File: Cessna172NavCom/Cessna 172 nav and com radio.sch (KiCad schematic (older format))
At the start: 33 parts, among them J2 USB_B_Micro, J8 Conn_02x20_Odd_Even, SW1 SW_Push, SW2 SW_Push, SW3 SW_Push, SW4 SW_Push, SW5 SW_Push, SW6 SW_Push

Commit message: Fully routed!!!
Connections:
- net GND: now also J8.27 (Pin_27), J8.28 (Pin_28), J8.29 (Pin_29), J8.30 (Pin_30)
- no-connect marks 11 -> 7
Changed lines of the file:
@@
 	1    0    0    -1
 $EndComp
-NoConn ~ 8650 1500
-NoConn ~ 8750 1500
-NoConn ~ 8750 2000
-NoConn ~ 8650 2000
 $Comp
-L power:+5V #PWR?
+L power:+5V #PWR0101
 U 1 1 5F695056
 P 2050 3500
-F 0 "#PWR?" H 2050 3350 50  0001 C CNN
+F 0 "#PWR0101" H 2050 3350 50  0001 C CNN
 F 1 "+5V" V 2065 3628 50  0000 L CNN
 F 2 "" H 2050 3500 50  0001 C CNN
@@
 $EndComp
 $Comp
-L power:GND #PWR?
+L power:GND #PWR0102
 U 1 1 5F6951C0
 P 2050 3800
-F 0 "#PWR?" H 2050 3550 50  0001 C CNN
+F 0 "#PWR0102" H 2050 3550 50  0001 C CNN
 F 1 "GND" V 2055 3672 50  0000 R CNN
 F 2 "" H 2050 3800 50  0001 C CNN
@@
 	0    1    1    0
 $EndComp
+$Comp
+L power:GND #PWR?
+U 1 1 5F67D432
+P 8650 1500
+F 0 "#PWR?" H 8650 1250 50  0001 C CNN
+F 1 "GND" H 8655 1327 50  0000 C CNN
+F 2 "" H 8650 1500 50  0001 C CNN
+F 3 "" H 8650 1500 50  0001 C CNN
+	1    8650 1500
+	-1   0    0    1
+$EndComp
+$Comp
+L power:GND #PWR?
+U 1 1 5F67D9D0
+P 8750 1450
+F 0 "#PWR?" H 8750 1200 50  0001 C CNN
+F 1 "GND" H 8755 1277 50  0000 C CNN
+F 2 "" H 8750 1450 50  0001 C CNN
+F 3 "" H 8750 1450 50  0001 C CNN
+	1    8750 1450
+	-1   0    0    1
+$EndComp
+$Comp
+L power:GND #PWR?
+U 1 1 5F67E0C2
+P 8650 2000
+F 0 "#PWR?" H 8650 1750 50  0001 C CNN
+F 1 "GND" H 8655 1827 50  0000 C CNN
+F 2 "" H 8650 2000 50  0001 C CNN
+F 3 "" H 8650 2000 50  0001 C CNN
+	1    8650 2000
+	1    0    0    -1
+$EndComp
+$Comp
+L power:GND #PWR?
+U 1 1 5F67E6E9
+P 8750 2050
+F 0 "#PWR?" H 8750 1800 50  0001 C CNN
+F 1 "GND" H 8755 1877 50  0000 C CNN
+F 2 "" H 8750 2050 50  0001 C CNN
+F 3 "" H 8750 2050 50  0001 C CNN
+	1    8750 2050
+	1    0    0    -1
+$EndComp
+Wire Wire Line
+	8750 2050 8750 2000
+Wire Wire Line
+	8750 1450 8750 1500
 $EndSCHEMATC

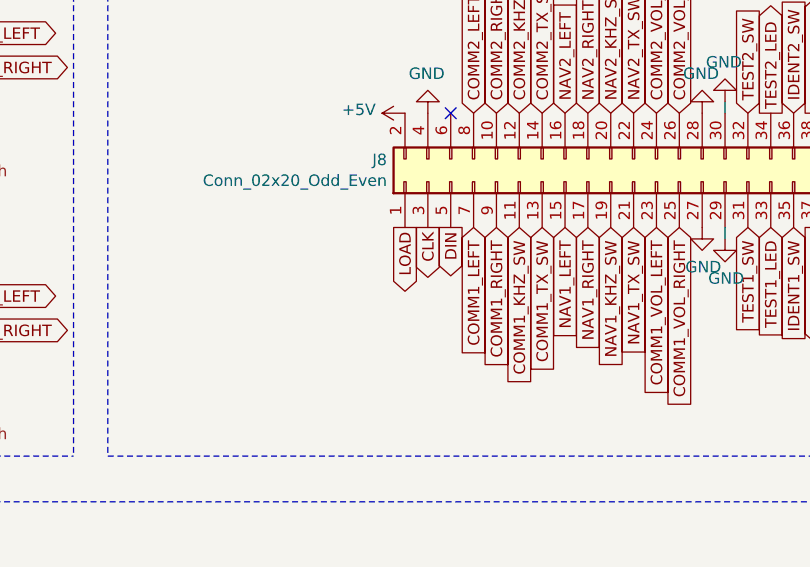
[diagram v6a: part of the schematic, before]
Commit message: Add mobiflight files, start Arduino shield
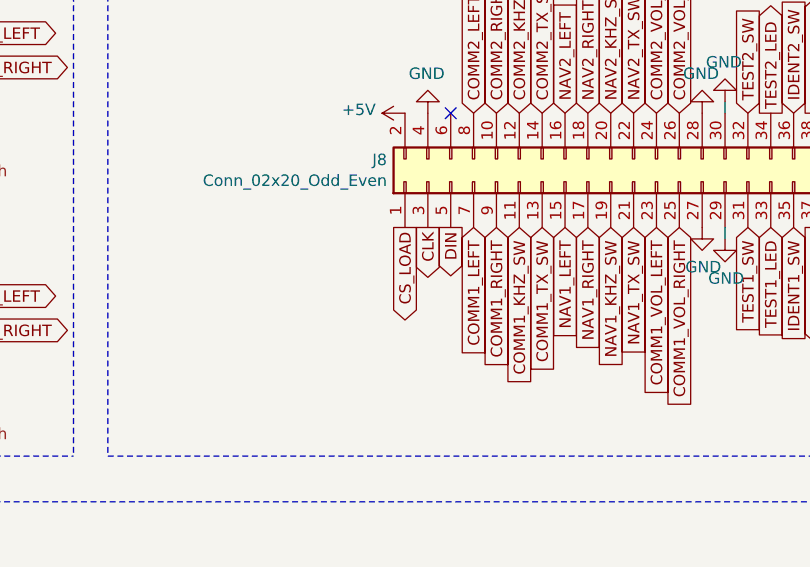
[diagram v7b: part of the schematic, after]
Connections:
- net LOAD: no longer J8.1 (Pin_1)
- new net CS_LOAD: J8.1 (Pin_1)
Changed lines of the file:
@@
 $EndComp
 Text GLabel 7350 2000 3    50   Output ~ 0
-LOAD
+CS_LOAD
 Text GLabel 7450 2000 3    50   Output ~ 0
 CLK

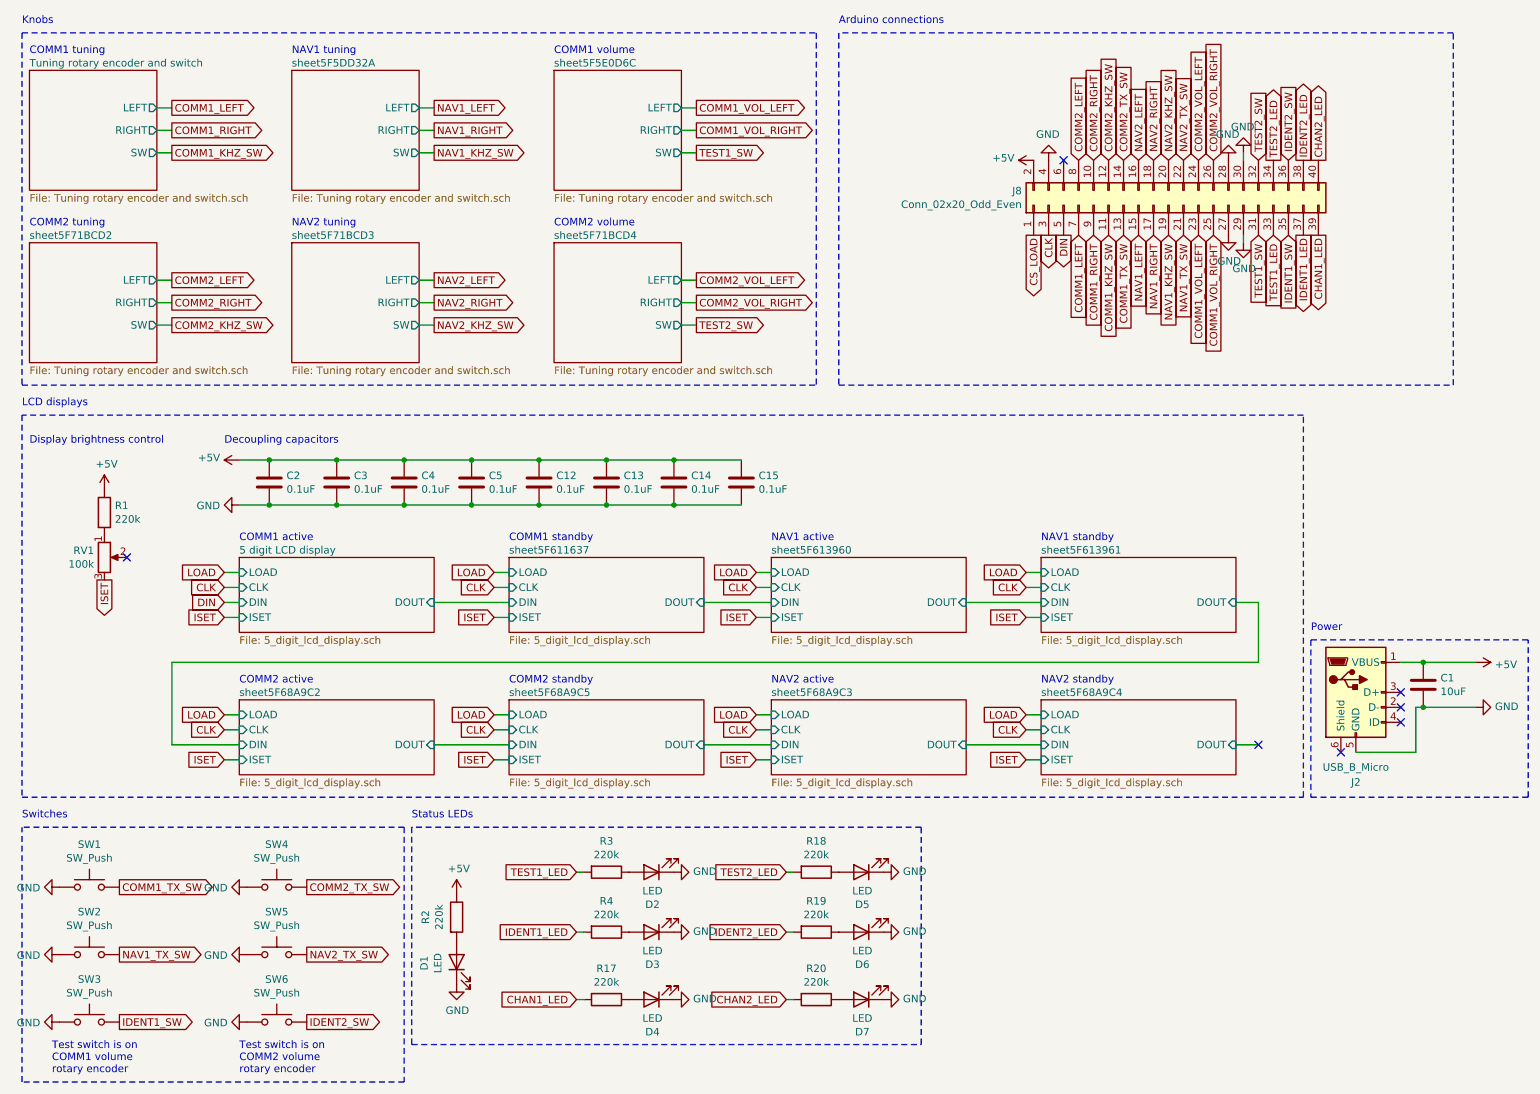
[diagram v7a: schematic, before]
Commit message: Remaining encoders and some buttons confirmed
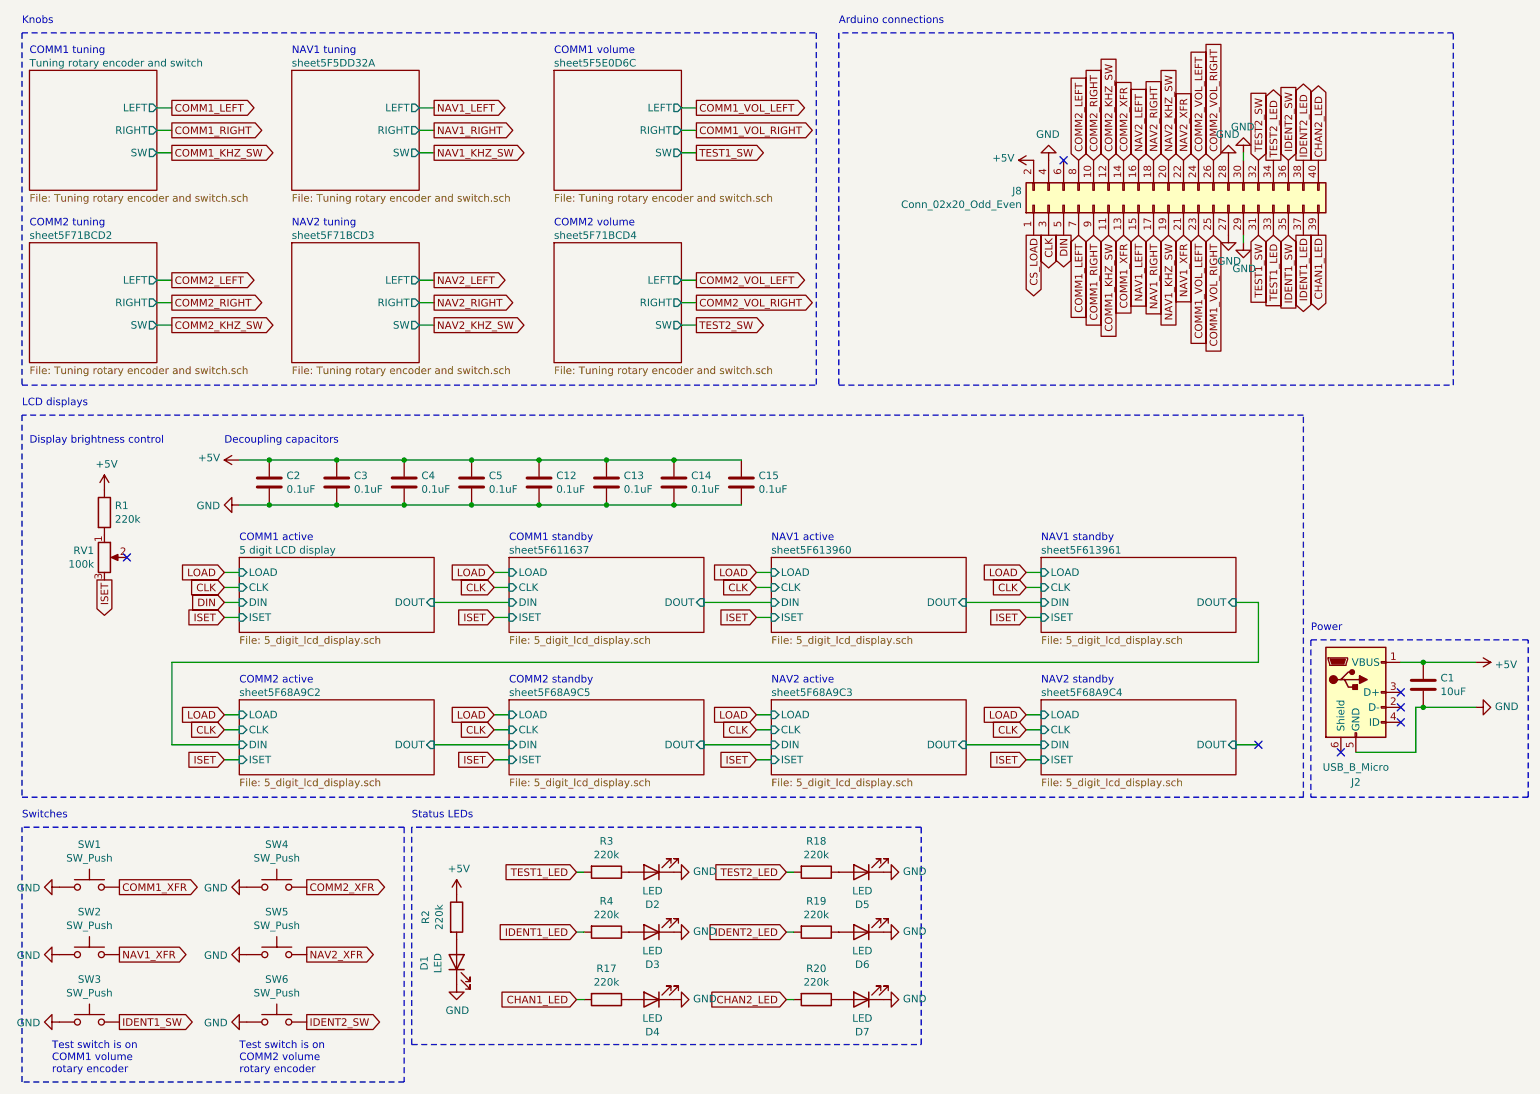
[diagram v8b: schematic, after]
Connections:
- net COMM1_TX_SW renamed COMM1_XFR
- net COMM2_TX_SW renamed COMM2_XFR
- net NAV1_TX_SW renamed NAV1_XFR
- net NAV2_TX_SW renamed NAV2_XFR
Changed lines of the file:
@@
 Connection ~ 3150 3800
 Text GLabel 1250 6350 2    50   Output ~ 0
-COMM1_TX_SW
+COMM1_XFR
 Text GLabel 1250 6800 2    50   Output ~ 0
-NAV1_TX_SW
+NAV1_XFR
 Text Notes 4150 800  0    50   ~ 0
 COMM1 volume
@@
 	1600 5400 2050 5400
 Text GLabel 2500 6350 2    50   Output ~ 0
-COMM2_TX_SW
+COMM2_XFR
 Text GLabel 2500 6800 2    50   Output ~ 0
-NAV2_TX_SW
+NAV2_XFR
 Text GLabel 2500 7250 2    50   Output ~ 0
 IDENT2_SW
@@
 TEST1_SW
 Text GLabel 7950 2000 3    50   Input ~ 0
-COMM1_TX_SW
+COMM1_XFR
 Text GLabel 8350 2000 3    50   Input ~ 0
-NAV1_TX_SW
+NAV1_XFR
 Text GLabel 9050 2000 3    50   Input ~ 0
 IDENT1_SW
@@
 COMM2_KHZ_SW
 Text GLabel 7950 1500 1    50   Input ~ 0
-COMM2_TX_SW
+COMM2_XFR
 Text GLabel 8050 1500 1    50   Input ~ 0
 NAV2_LEFT
@@
 NAV2_KHZ_SW
 Text GLabel 8350 1500 1    50   Input ~ 0
-NAV2_TX_SW
+NAV2_XFR
 Text GLabel 8450 1500 1    50   Input ~ 0
 COMM2_VOL_LEFT
